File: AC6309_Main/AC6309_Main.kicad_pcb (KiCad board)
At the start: 2 copper layers, 19 parts, among them J1 Address, J2 Data and Control, J3 FTDI Header, SW1 Reset, U1 HD63B09P, U2 W24257, U3 28C256, U4 MC68B50, U5 74HCT00, U6 74HC138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

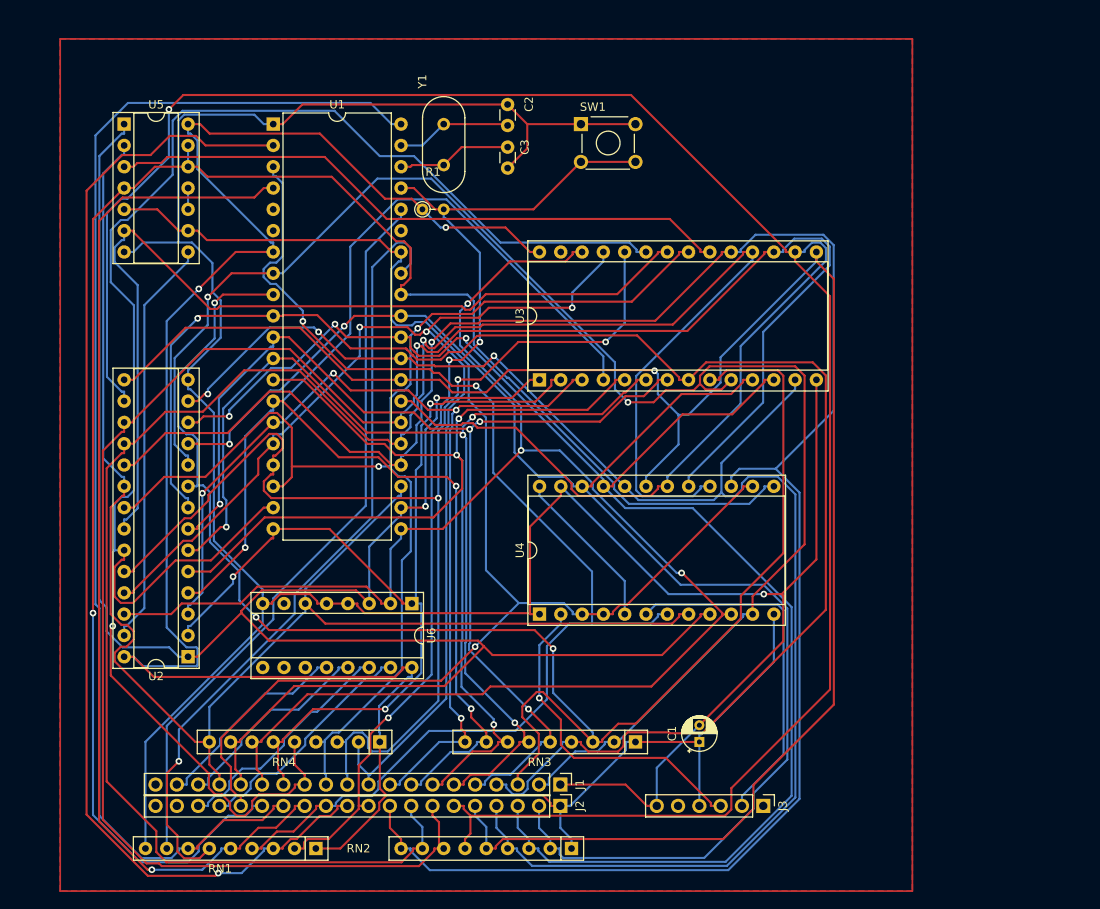
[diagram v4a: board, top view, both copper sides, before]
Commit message: SCH and PCB updats. DRC issues fixed.
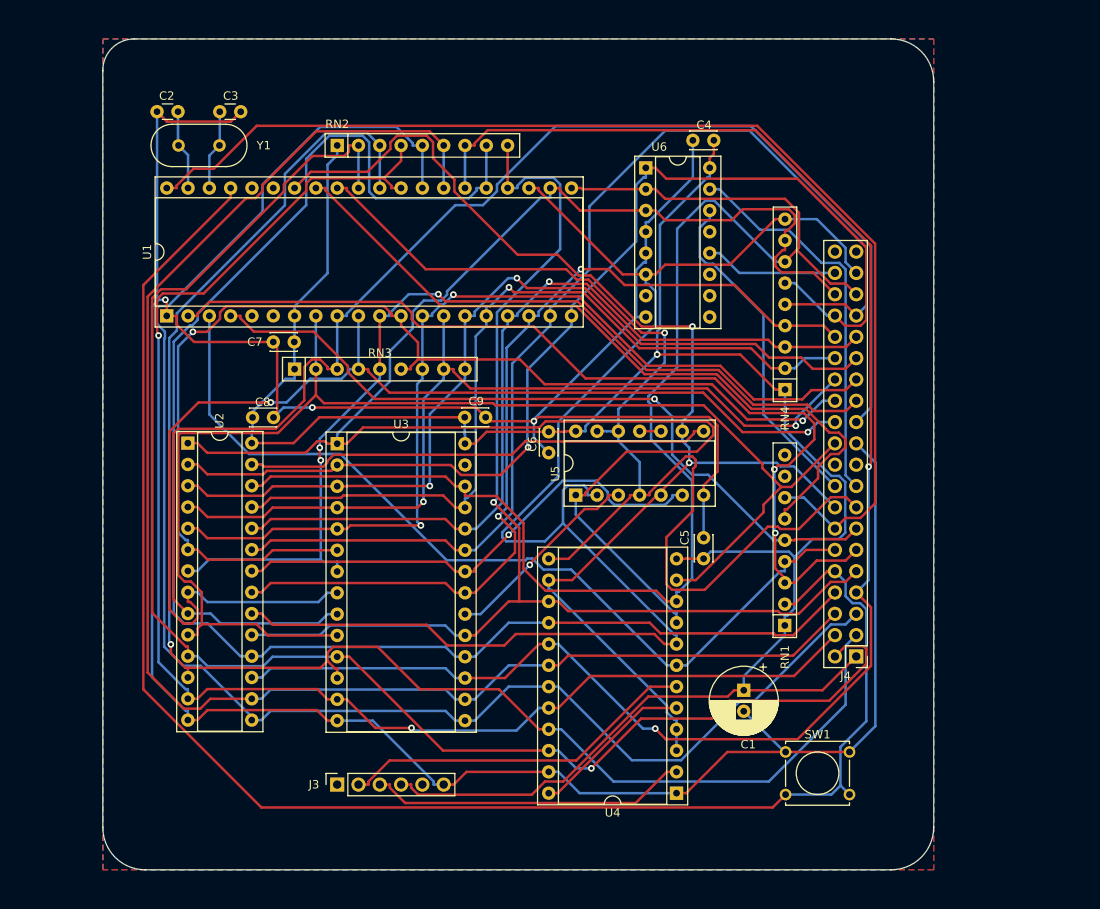
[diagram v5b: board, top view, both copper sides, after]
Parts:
- removed J1: Address, Connector_PinHeader_2.54mm:PinHeader_1x20_P2.54mm_Vertical
- removed J2: Data and Control, Connector_PinHeader_2.54mm:PinHeader_1x20_P2.54mm_Vertical
- removed R1: 2K2, Resistor_THT:R_Axial_DIN0204_L3.6mm_D1.6mm_P2.54mm_Vertical
- added C4: 100 nF, Capacitor_THT:C_Disc_D3.0mm_W2.0mm_P2.50mm, F.Cu at (123.6, 37.5)
- added C5: 100 nF, Capacitor_THT:C_Disc_D3.0mm_W2.0mm_P2.50mm, F.Cu at (122.4, 87.4)
- added C6: 100 nF, Capacitor_THT:C_Disc_D3.0mm_W2.0mm_P2.50mm, F.Cu at (104.0, 72.2)
- added C7: 100 nF, Capacitor_THT:C_Disc_D3.0mm_W2.0mm_P2.50mm, F.Cu at (73.6, 61.5)
- added C8: 100 nF, Capacitor_THT:C_Disc_D3.0mm_W2.0mm_P2.50mm, F.Cu at (68.6, 70.5)
- added C9: 100 nF, Capacitor_THT:C_Disc_D3.0mm_W2.0mm_P2.50mm, F.Cu at (93.9, 70.5)
- added J4: Conn_IO, Connector_PinHeader_2.54mm:PinHeader_2x20_P2.54mm_Vertical, F.Cu at (140.6, 99.0)
- C1: footprint Capacitor_THT:CP_Radial_D4.0mm_P2.00mm -> Capacitor_THT:CP_Radial_D8.0mm_P2.50mm
- J3: footprint Connector_PinHeader_2.54mm:PinHeader_1x06_P2.54mm_Vertical -> Connector_PinSocket_2.54mm:PinSocket_1x06_P2.54mm_Vertical
- SW1: footprint Button_Switch_THT:SW_TH_Tactile_Omron_B3F-10xx -> Button_Switch_THT:SW_Tactile_Straight_KSL0Axx1LFTR
- U1: footprint Package_DIP:DIP-40_W15.24mm -> Package_DIP:DIP-40_W15.24mm_Socket
- U4: value MC68B50 -> HD63B50
- moved RN2 88.4 mm to (78.7, 38.1), turned to 0 degrees
- moved SW1 78.7 mm to (132.2, 110.4)
- moved U5 69.7 mm to (107.2, 79.8), turned to 90 degrees
- moved RN4 64.0 mm to (132.1, 67.2), turned to 90 degrees
- moved RN1 61.9 mm to (132.1, 95.3), turned to 90 degrees
- moved RN3 60.2 mm to (73.7, 64.8), turned to 0 degrees
- moved U6 59.0 mm to (115.5, 40.8), turned to 0 degrees
- moved J3 50.9 mm to (78.7, 114.3), turned to 90 degrees
- moved C2 39.3 mm to (59.8, 34.1), turned to 180 degrees
- moved C3 34.6 mm to (64.7, 34.1), turned to 0 degrees
- moved U4 26.9 mm to (119.2, 115.3), turned to 180 degrees
- moved Y1 26.8 mm to (64.7, 38.1), turned to 180 degrees
- moved U1 26.1 mm to (58.4, 58.4), turned to 90 degrees
- moved U2 25.5 mm to (60.9, 73.6), turned to 0 degrees
- moved U3 25.3 mm to (78.7, 73.7), turned to 0 degrees
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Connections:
- net /C000_CS renamed //C000_CS_ROM
- net Net-(J3-Pin_2) renamed /ACIA_TX
- net Net-(J3-Pin_3) renamed /ACIA_RX
- RN1 pad 8: /MRDY -> unconnected-(RN1-R7-Pad8)
- RN1 pad 9: GND -> unconnected-(RN1-R8-Pad9)
- U1 pad 36: /MRDY -> unconnected-(U1-MRDY-Pad36)
- U6 pad 12: /B000_CS -> //B000_CS
- U6 pad 13: /A000_CS -> //A000_CS_ACIA
- U6 pad 14: /9000_CS -> //9000_CS
- U6 pad 15: /8000_CS -> //8000_CS
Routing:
- net /D4: track 312.4 -> 183.9 mm, vias 1 -> 0
- net /D7: track 245.4 -> 144.0 mm
- net /MRDY: track 87.9 -> 0.00 mm
- net /A11: track 207.1 -> 134.6 mm, vias 1 -> 0
- net /R/W: track 209.4 -> 139.1 mm
- net //RESET: track 122.9 -> 192.2 mm, vias 3 -> 0
- net /A6: track 163.4 -> 104.9 mm, vias 3 -> 2
- net /D6: track 233.5 -> 182.2 mm, vias 1 -> 0
- net //READ: track 110.2 -> 59.2 mm, vias 0 -> 1
- net //ROM_CS: track 75.2 -> 24.4 mm, vias 0 -> 1
- net /A8: track 145.7 -> 98.8 mm, vias 3 -> 1
- net //8000_CS: track 0.00 -> 46.5 mm
- net /A2: track 187.0 -> 140.9 mm, vias 1 -> 2
- net /A14: track 242.1 -> 196.5 mm, vias 2 -> 0
- net /A9: track 147.4 -> 101.8 mm, vias 3 -> 1
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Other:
- board outline added: 99.1 x 99.1 mm

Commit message: Updates from 2024. Rev1 going in production.
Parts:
- J1: renamed from J4; value Conn_IO -> I/O
- J2: renamed from J3; value FTDI Header -> FTDI
- U5: value 74HCT00 -> 74HC00
- moved C2 72.8 mm to (132.6, 34.0), turned to 90 degrees
- moved C3 68.0 mm to (132.6, 38.9), turned to -90 degrees
- moved C4 66.5 mm to (86.8, 92.9), turned to -90 degrees
- moved U6 65.4 mm to (76.0, 92.9)
- moved Y1 63.8 mm to (128.5, 38.9), turned to 90 degrees
- moved SW1 61.1 mm to (134.4, 49.4), turned to 180 degrees
- moved U1 56.1 mm to (108.2, 32.6), turned to 0 degrees
- moved RN2 55.2 mm to (131.9, 53.0), turned to -90 degrees
- moved U5 49.3 mm to (59.7, 92.8), turned to 0 degrees
- moved J1 46.3 mm to (136.0, 53.0), turned to 0 degrees
- moved C6 39.5 mm to (70.3, 92.8)
- moved C9 37.1 mm to (57.0, 73.8), turned to 90 degrees
- moved C7 34.7 mm to (105.0, 46.9), turned to 90 degrees
- moved J2 34.6 mm to (113.3, 112.0), turned to -90 degrees
- moved RN3 34.4 mm to (104.6, 49.9), turned to -90 degrees
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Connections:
- J1 pad 10: //RESET -> /A3
- J1 pad 11: //NMI -> /D4
- J1 pad 12: //IRQ -> /A4
- J1 pad 13: //FIRQ -> /D5
- J1 pad 14: //HALT -> /A5
- J1 pad 15: /R/W -> /D6
- J1 pad 16: /E -> /A6
- J1 pad 17: //8000_CS -> /D7
- J1 pad 18: //9000_CS -> /A7
- J1 pad 19: unconnected-(J4-Pin_19-Pad19) -> //RESET
- J1 pad 2: /D0 -> GND
- J1 pad 20: unconnected-(J4-Pin_20-Pad20) -> /A8
- J1 pad 21: GND -> //NMI
- J1 pad 22: /A0 -> /A9
- J1 pad 23: /A1 -> //IRQ
- J1 pad 24: /A2 -> /A10
- J1 pad 25: /A3 -> //FIRQ
- J1 pad 26: /A4 -> /A11
- J1 pad 27: /A5 -> //HALT
- J1 pad 28: /A6 -> /A12
- J1 pad 29: /A7 -> /R/W
- J1 pad 3: /D1 -> /D0
- J1 pad 30: /A8 -> /A13
- J1 pad 31: /A9 -> /E
- J1 pad 32: /A10 -> /A14
- J1 pad 33: /A11 -> //8000_CS
- J1 pad 34: /A12 -> /A15
- J1 pad 35: /A13 -> //9000_CS
- J1 pad 36: /A14 -> //B000_CS
- J1 pad 37: /A15 -> unconnected-(J1-Pin_37-Pad37)
- J1 pad 38: //B000_CS -> unconnected-(J1-Pin_38-Pad38)
- J1 pad 4: /D2 -> /A0
- J1 pad 5: /D3 -> /D1
- J1 pad 6: /D4 -> /A1
- J1 pad 7: /D5 -> /D2
- J1 pad 8: /D6 -> /A2
- J1 pad 9: /D7 -> /D3
- J2 pad 2: /ACIA_TX -> /ACIA_RX
- J2 pad 3: /ACIA_RX -> /ACIA_TX
- RN1 pad 6: //DMABREQ -> //HALT
- RN1 pad 7: //HALT -> //DMABREQ
- U1 pad 35: /Q -> unconnected-(U1-Q-Pad35)
- U6 pad 11: //C000_CS_ROM -> unconnected-(U6-~{Y4}-Pad11)
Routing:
- net GND: track 361.7 -> 0.00 mm, vias 3 -> 0
- net VCC: track 266.2 -> 424.8 mm, vias 1 -> 0
- net //RESET: track 192.2 -> 58.0 mm, vias 0 -> 1
- net /A1: track 174.6 -> 66.2 mm
- net /A2: track 140.9 -> 66.2 mm, vias 2 -> 0
- net /A4: track 135.7 -> 66.2 mm, vias 2 -> 0
- net /D1: track 188.0 -> 125.4 mm
- net /D5: track 196.4 -> 135.0 mm, vias 2 -> 1
- net /D0: track 181.4 -> 125.3 mm, vias 1 -> 0
- net //HALT: track 138.0 -> 83.4 mm, vias 0 -> 2
- net /D6: track 182.2 -> 131.6 mm, vias 0 -> 1
- net /D2: track 174.7 -> 124.9 mm, vias 2 -> 1
- net /A3: track 116.0 -> 66.3 mm, vias 3 -> 0
- net /D3: track 189.5 -> 141.7 mm, vias 0 -> 1
- net /A5: track 113.4 -> 66.3 mm, vias 2 -> 0
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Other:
- board text added: "2024 Dimitar Angelov http://github.com/izne/AC6309/"
- board text added: "7.3728MHz"
- board text added: "A0"
- board text added: "AC29/AC6309 - rev.1"
- board text added: "GND"
- board text added: "RX"
- board text added: "TX"
- board text added: "VCC"
